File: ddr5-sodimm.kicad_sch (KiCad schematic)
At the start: 0 parts

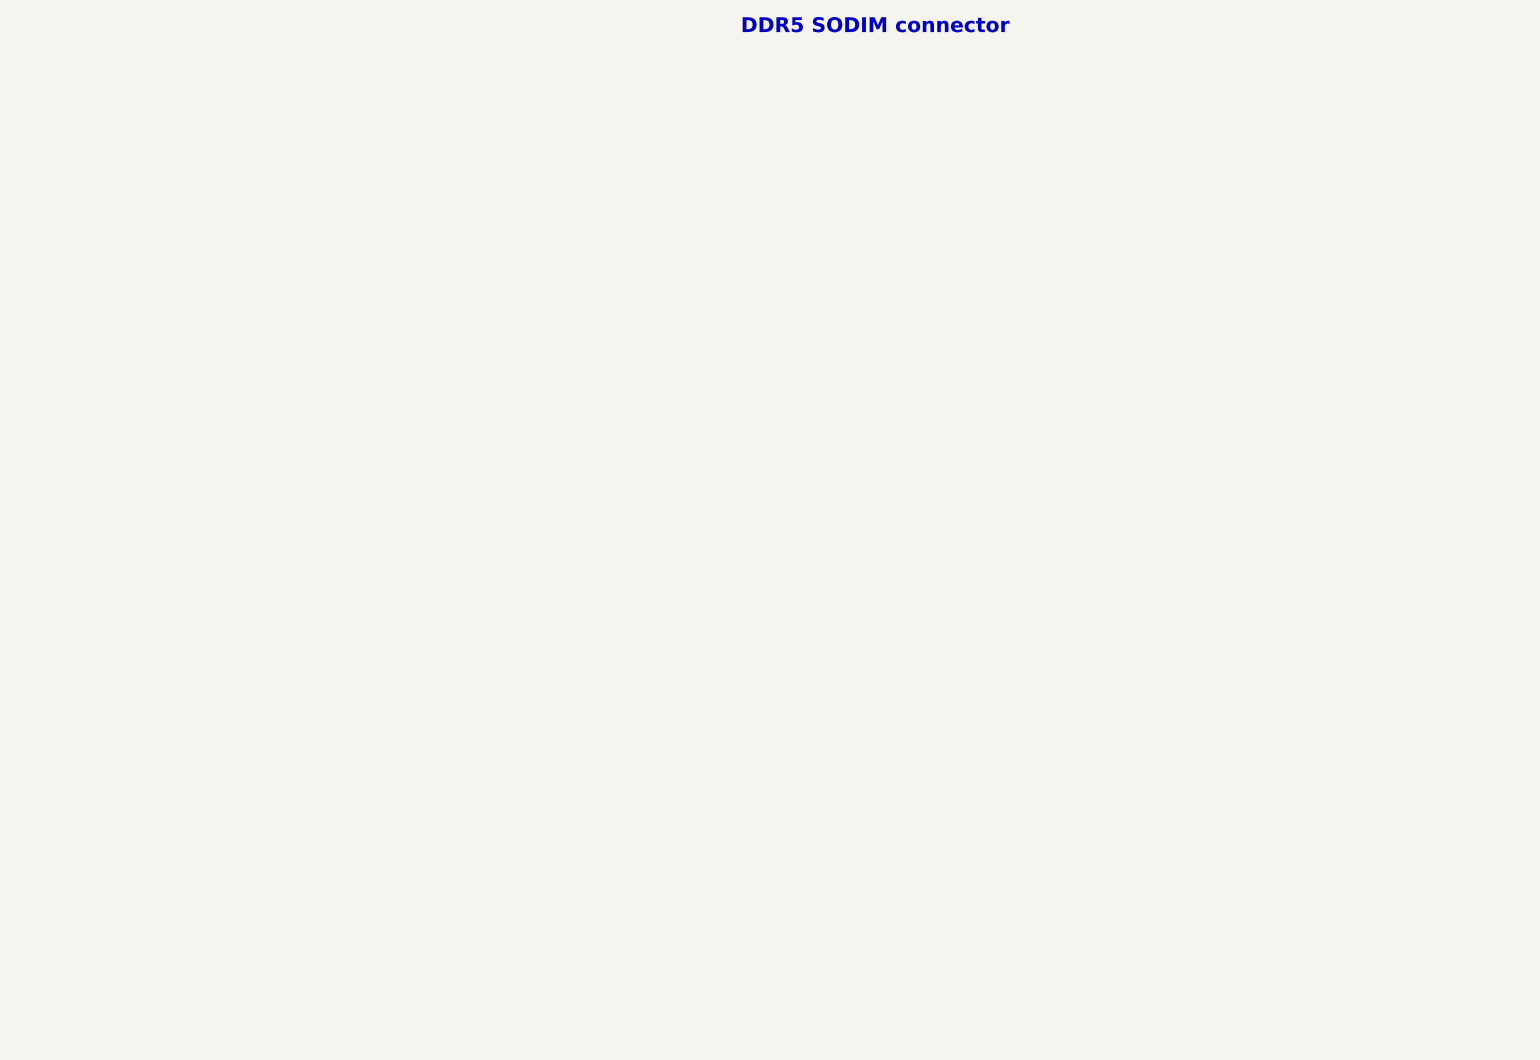
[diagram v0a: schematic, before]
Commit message: Add DDR5 connector to the schematic
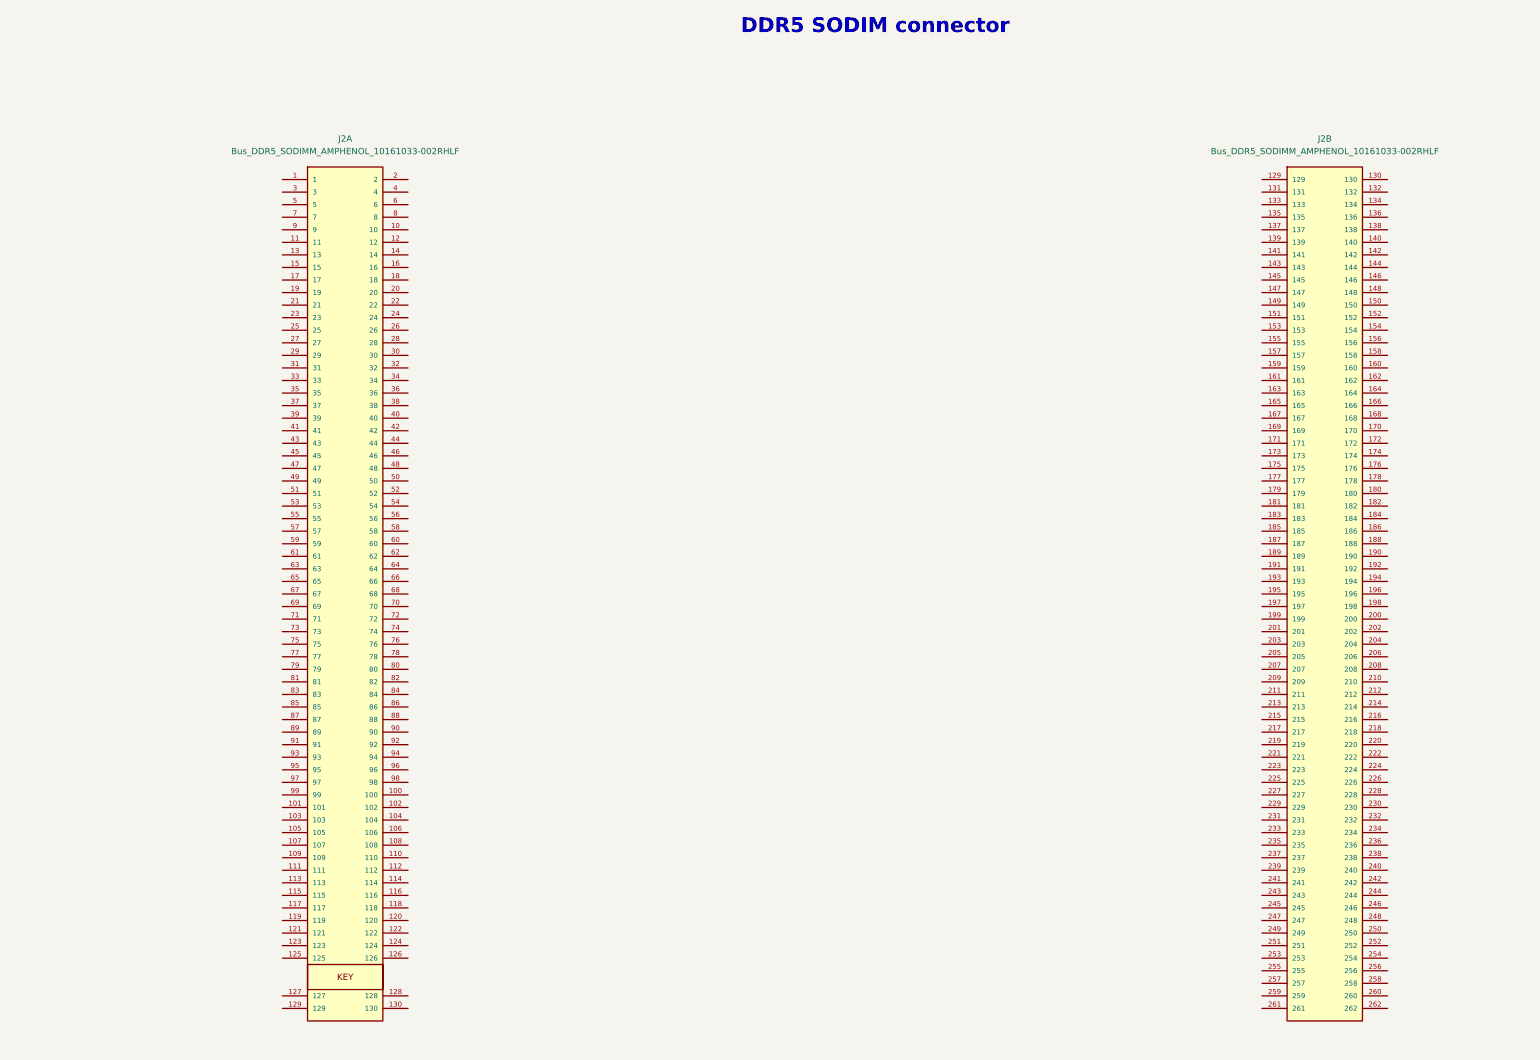
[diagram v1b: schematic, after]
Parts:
- added J2: Bus_DDR5_SODIMM_AMPHENOL_10161033-002RHLF, antmicro-footprints:DDR5_AMPHENOL_10161033-002RHLF, symbol antmicroMemoryConnectorsPCCardSockets:Bus_DDR5_SODIMM_AMPHENOL_10161033-002RHLF

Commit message: Update DDR5 SO-DIMM symbol and connect signals
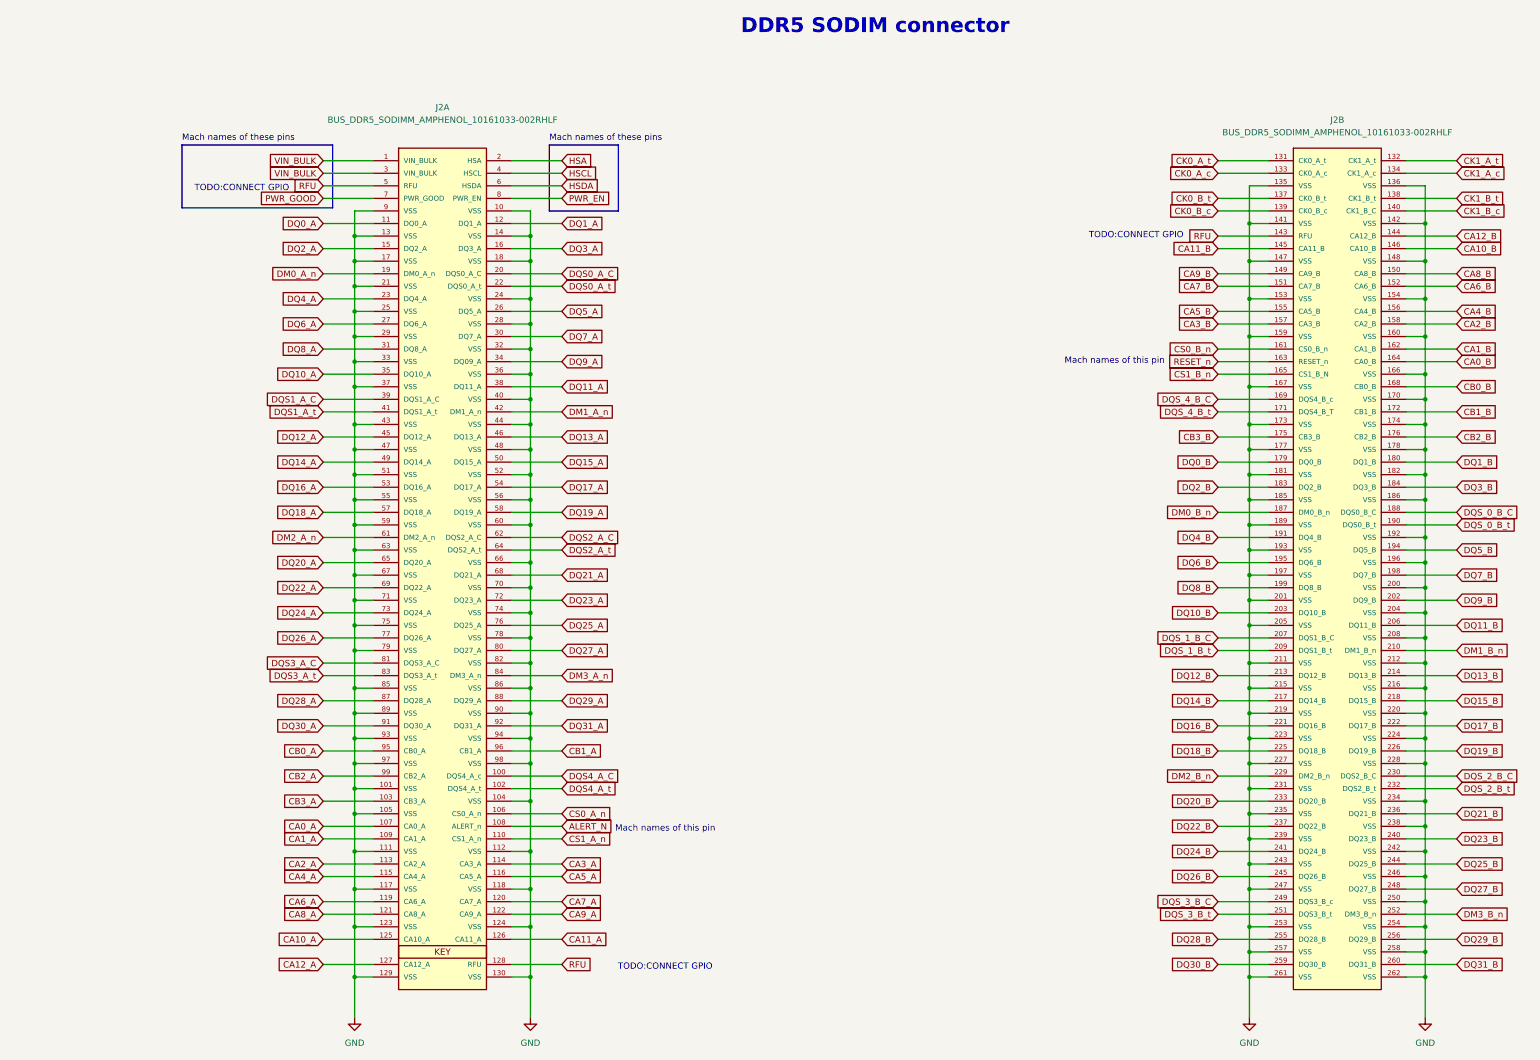
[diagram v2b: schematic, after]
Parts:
- removed J2: Bus_DDR5_SODIMM_AMPHENOL_10161033-002RHLF, antmicro-footprints:DDR5_AMPHENOL_10161033-002RHLF, symbol antmicroMemoryConnectorsPCCardSockets:Bus_DDR5_SODIMM_AMPHENOL_10161033-002RHLF
- added J2: BUS_DDR5_SODIMM_AMPHENOL_10161033-002RHLF, antmicro-footprints:DDR5_AMPHENOL_10161033-002RHLF, symbol antmicroMemoryConnectorsPCCardSockets:BUS_DDR5_SODIMM_AMPHENOL_10161033-002RHLF
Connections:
- new net ALERT_N: J2.108 (ALERT_n)
- new net CA0_A: J2.107 (CA0_A)
- new net CA0_B: J2.164 (CA0_B)
- new net CA10_A: J2.125 (CA10_A)
- new net CA10_B: J2.146 (CA10_B)
- new net CA11_A: J2.126 (CA11_A)
- new net CA11_B: J2.145 (CA11_B)
- new net CA12_A: J2.127 (CA12_A)
- new net CA12_B: J2.144 (CA12_B)
- new net CA1_A: J2.109 (CA1_A)
- new net CA1_B: J2.162 (CA1_B)
- new net CA2_A: J2.113 (CA2_A)
- new net CA2_B: J2.158 (CA2_B)
- new net CA3_A: J2.114 (CA3_A)
- new net CA3_B: J2.157 (CA3_B)
- new net CA4_A: J2.115 (CA4_A)
- new net CA4_B: J2.156 (CA4_B)
- new net CA5_A: J2.116 (CA5_A)
- new net CA5_B: J2.155 (CA5_B)
- new net CA6_A: J2.119 (CA6_A)
- new net CA6_B: J2.152 (CA6_B)
- new net CA7_A: J2.120 (CA7_A)
- new net CA7_B: J2.151 (CA7_B)
- new net CA8_A: J2.121 (CA8_A)
- new net CA8_B: J2.150 (CA8_B)
- new net CA9_A: J2.122 (CA9_A)
- new net CA9_B: J2.149 (CA9_B)
- new net CB0_A: J2.95 (CB0_A)
- new net CB0_B: J2.168 (CB0_B)
- new net CB1_A: J2.96 (CB1_A)
- new net CB1_B: J2.172 (CB1_B)
- new net CB2_A: J2.99 (CB2_A)
- new net CB2_B: J2.176 (CB2_B)
- new net CB3_A: J2.103 (CB3_A)
- new net CB3_B: J2.175 (CB3_B)
- new net CK0_A_c: J2.133 (CK0_A_c)
- new net CK0_A_t: J2.131 (CK0_A_t)
- new net CK0_B_c: J2.139 (CK0_B_c)
- new net CK0_B_t: J2.137 (CK0_B_t)
- new net CK1_A_c: J2.134 (CK1_A_c)
- new net CK1_A_t: J2.132 (CK1_A_t)
- new net CK1_B_c: J2.140 (CK1_B_C)
- new net CK1_B_t: J2.138 (CK1_B_t)
- new net CS0_A_n: J2.106 (CS0_A_n)
- new net CS0_B_n: J2.161 (CS0_B_n)
- new net CS1_A_n: J2.110 (CS1_A_n)
- new net CS1_B_n: J2.165 (CS1_B_N)
- new net DM0_A_n: J2.19 (DM0_A_n)
- new net DM0_B_n: J2.187 (DM0_B_n)
- new net DM1_A_n: J2.42 (DM1_A_n)
- new net DM1_B_n: J2.210 (DM1_B_n)
- new net DM2_A_n: J2.61 (DM2_A_n)
- new net DM2_B_n: J2.229 (DM2_B_n)
- new net DM3_A_n: J2.84 (DM3_A_n)
- new net DM3_B_n: J2.252 (DM3_B_n)
- new net DQ0_A: J2.11 (DQ0_A)
- new net DQ0_B: J2.179 (DQ0_B)
- new net DQ10_A: J2.35 (DQ10_A)
- new net DQ10_B: J2.203 (DQ10_B)
- new net DQ11_A: J2.38 (DQ11_A)
- new net DQ11_B: J2.206 (DQ11_B)
- new net DQ12_A: J2.45 (DQ12_A)
- new net DQ12_B: J2.213 (DQ12_B)
- new net DQ13_A: J2.46 (DQ13_A)
- new net DQ13_B: J2.214 (DQ13_B)
- new net DQ14_A: J2.49 (DQ14_A)
- new net DQ14_B: J2.217 (DQ14_B)
- new net DQ15_A: J2.50 (DQ15_A)
- new net DQ15_B: J2.218 (DQ15_B)
- new net DQ16_A: J2.53 (DQ16_A)
- new net DQ16_B: J2.221 (DQ16_B)
- new net DQ17_A: J2.54 (DQ17_A)
- new net DQ17_B: J2.222 (DQ17_B)
- new net DQ18_A: J2.57 (DQ18_A)
- new net DQ18_B: J2.225 (DQ18_B)
- new net DQ19_A: J2.58 (DQ19_A)
- new net DQ19_B: J2.226 (DQ19_B)
- new net DQ1_A: J2.12 (DQ1_A)
- new net DQ1_B: J2.180 (DQ1_B)
- new net DQ20_A: J2.65 (DQ20_A)
- new net DQ20_B: J2.233 (DQ20_B)
- new net DQ21_A: J2.68 (DQ21_A)
- new net DQ21_B: J2.236 (DQ21_B)
- new net DQ22_A: J2.69 (DQ22_A)
- new net DQ22_B: J2.237 (DQ22_B)
- new net DQ23_A: J2.72 (DQ23_A)
- new net DQ23_B: J2.240 (DQ23_B)
- new net DQ24_A: J2.73 (DQ24_A)
- new net DQ24_B: J2.241 (DQ24_B)
- new net DQ25_A: J2.76 (DQ25_A)
- new net DQ25_B: J2.244 (DQ25_B)
- new net DQ26_A: J2.77 (DQ26_A)
- new net DQ26_B: J2.245 (DQ26_B)
- new net DQ27_A: J2.80 (DQ27_A)
- new net DQ27_B: J2.248 (DQ27_B)
- new net DQ28_A: J2.87 (DQ28_A)
- new net DQ28_B: J2.255 (DQ28_B)
- new net DQ29_A: J2.88 (DQ29_A)
- new net DQ29_B: J2.256 (DQ29_B)
- new net DQ2_A: J2.15 (DQ2_A)
- new net DQ2_B: J2.183 (DQ2_B)
- new net DQ30_A: J2.91 (DQ30_A)
- new net DQ30_B: J2.259 (DQ30_B)
- new net DQ31_A: J2.92 (DQ31_A)
- new net DQ31_B: J2.260 (DQ31_B)
- new net DQ3_A: J2.16 (DQ3_A)
- new net DQ3_B: J2.184 (DQ3_B)
- new net DQ4_A: J2.23 (DQ4_A)
- new net DQ4_B: J2.191 (DQ4_B)
- new net DQ5_A: J2.26 (DQ5_A)
- new net DQ5_B: J2.194 (DQ5_B)
- new net DQ6_A: J2.27 (DQ6_A)
- new net DQ6_B: J2.195 (DQ6_B)
- new net DQ7_A: J2.30 (DQ7_A)
- new net DQ7_B: J2.198 (DQ7_B)
- new net DQ8_A: J2.31 (DQ8_A)
- new net DQ8_B: J2.199 (DQ8_B)
- new net DQ9_A: J2.34 (DQ09_A)
- new net DQ9_B: J2.202 (DQ9_B)
- new net DQS0_A_C: J2.20 (DQS0_A_C)
- new net DQS0_A_t: J2.22 (DQS0_A_t)
- new net DQS1_A_C: J2.39 (DQS1_A_C)
- new net DQS1_A_t: J2.41 (DQS1_A_t)
- new net DQS2_A_C: J2.62 (DQS2_A_C)
- new net DQS2_A_t: J2.64 (DQS2_A_t)
- new net DQS3_A_C: J2.81 (DQS3_A_C)
- new net DQS3_A_t: J2.83 (DQS3_A_t)
- new net DQS4_A_C: J2.100 (DQS4_A_c)
- new net DQS4_A_t: J2.102 (DQS4_A_t)
- new net DQS_0_B_C: J2.188 (DQS0_B_C)
- new net DQS_0_B_t: J2.190 (DQS0_B_t)
- new net DQS_1_B_C: J2.207 (DQS1_B_C)
- new net DQS_1_B_t: J2.209 (DQS1_B_t)
- new net DQS_2_B_C: J2.230 (DQS2_B_C)
- new net DQS_2_B_t: J2.232 (DQS2_B_t)
- new net DQS_3_B_C: J2.249 (DQS3_B_c)
- new net DQS_3_B_t: J2.251 (DQS3_B_t)
- new net DQS_4_B_C: J2.169 (DQS4_B_c)
- new net DQS_4_B_t: J2.171 (DQS4_B_T)
- new net GND: J2.10 (VSS), J2.101 (VSS), J2.104 (VSS), J2.105 (VSS), J2.111 (VSS), J2.112 (VSS), J2.117 (VSS), J2.118 (VSS), J2.123 (VSS), J2.124 (VSS), J2.129 (VSS), J2.13 (VSS), J2.130 (VSS), J2.135 (VSS), J2.136 (VSS), J2.14 (VSS), J2.141 (VSS), J2.142 (VSS), J2.147 (VSS), J2.148 (VSS), J2.153 (VSS), J2.154 (VSS), J2.159 (VSS), J2.160 (VSS), J2.166 (VSS), J2.167 (VSS), J2.17 (VSS), J2.170 (VSS), J2.173 (VSS), J2.174 (VSS), J2.177 (VSS), J2.178 (VSS), J2.18 (VSS), J2.181 (VSS), J2.182 (VSS), J2.185 (VSS), J2.186 (VSS), J2.189 (VSS), J2.192 (VSS), J2.193 (VSS), J2.196 (VSS), J2.197 (VSS), J2.200 (VSS), J2.201 (VSS), J2.204 (VSS), J2.205 (VSS), J2.208 (VSS), J2.21 (VSS), J2.211 (VSS), J2.212 (VSS), J2.215 (VSS), J2.216 (VSS), J2.219 (VSS), J2.220 (VSS), J2.223 (VSS), J2.224 (VSS), J2.227 (VSS), J2.228 (VSS), J2.231 (VSS), J2.234 (VSS), J2.235 (VSS), J2.238 (VSS), J2.239 (VSS), J2.24 (VSS), J2.242 (VSS), J2.243 (VSS), J2.246 (VSS), J2.247 (VSS), J2.25 (VSS), J2.250 (VSS), J2.253 (VSS), J2.254 (VSS), J2.257 (VSS), J2.258 (VSS), J2.261 (VSS), J2.262 (VSS), J2.28 (VSS), J2.29 (VSS), J2.32 (VSS), J2.33 (VSS), J2.36 (VSS), J2.37 (VSS), J2.40 (VSS), J2.43 (VSS), J2.44 (VSS), J2.47 (VSS), J2.48 (VSS), J2.51 (VSS), J2.52 (VSS), J2.55 (VSS), J2.56 (VSS), J2.59 (VSS), J2.60 (VSS), J2.63 (VSS), J2.66 (VSS), J2.67 (VSS), J2.70 (VSS), J2.71 (VSS), J2.74 (VSS), J2.75 (VSS), J2.78 (VSS), J2.79 (VSS), J2.82 (VSS), J2.85 (VSS), J2.86 (VSS), J2.89 (VSS), J2.9 (VSS), J2.90 (VSS), J2.93 (VSS), J2.94 (VSS), J2.97 (VSS), J2.98 (VSS)
- new net HSA: J2.2 (HSA)
- new net HSCL: J2.4 (HSCL)
- new net HSDA: J2.6 (HSDA)
- new net PWR_EN: J2.8 (PWR_EN)
- new net PWR_GOOD: J2.7 (PWR_GOOD)
- new net RESET_n: J2.163 (RESET_n)
- new net RFU: J2.128 (RFU), J2.143 (RFU), J2.5 (RFU)
- new net VIN_BULK: J2.1 (VIN_BULK), J2.3 (VIN_BULK)
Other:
- note added: "Mach names of these pins"
- note added: "Mach names of this pin"
- note added: "TODO:CONNECT GPIO"

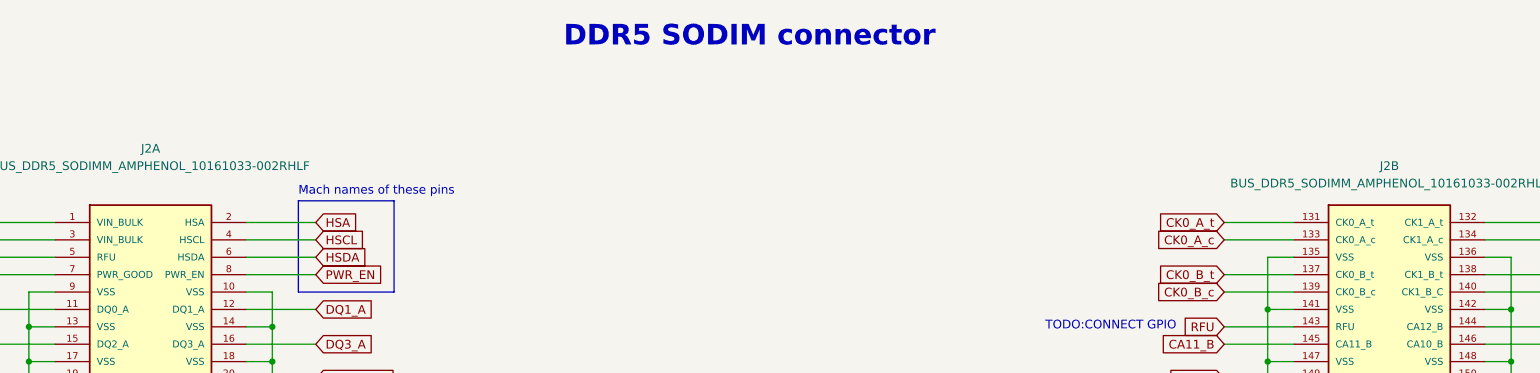
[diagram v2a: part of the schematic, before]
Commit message: Update designators and sync schematic with PCB
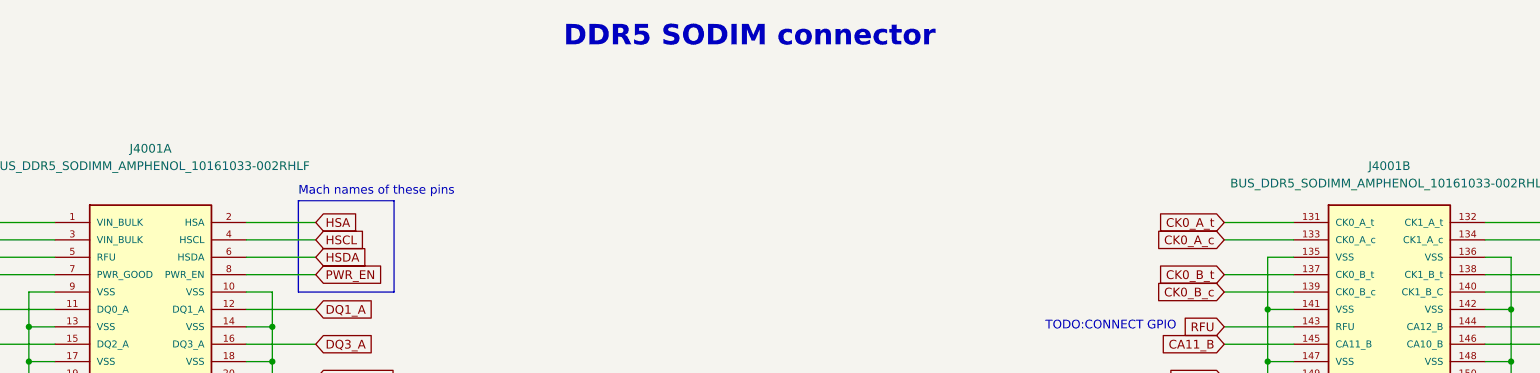
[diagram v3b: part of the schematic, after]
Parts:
- renumbered J2 to J4001
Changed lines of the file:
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@@
   (symbol (lib_id "data-center-rdimm-ddr4-tester:GND") (at 276.86 224.79 0) (unit 1)
     (in_bom yes) (on_board yes) (fields_autoplaced)
-    (property "Reference" "#PWR?" (id 0) (at 276.86 231.14 0)
+    (property "Reference" "#PWR04003" (id 0) (at 276.86 231.14 0)
       (effects (font (size 1.27 1.27)) hide)
     )
@@
   (symbol (lib_id "data-center-rdimm-ddr4-tester:GND") (at 95.885 224.79 0) (unit 1)
     (in_bom yes) (on_board yes) (fields_autoplaced)
-    (property "Reference" "#PWR?" (id 0) (at 95.885 231.14 0)
+    (property "Reference" "#PWR04001" (id 0) (at 95.885 231.14 0)
       (effects (font (size 1.27 1.27)) hide)
     )
@@
   (symbol (lib_name "BUS_DDR5_SODIMM_AMPHENOL_10161033-002RHLF_1") (lib_id "antmicroMemoryConnectorsPCCardSockets:BUS_DDR5_SODIMM_AMPHENOL_10161033-002RHLF") (at 294.64 130.175 0) (unit 2)
     (in_bom yes) (on_board yes) (fields_autoplaced)
-    (property "Reference" "J2" (id 0) (at 294.64 43.18 0))
+    (property "Reference" "J4001" (id 0) (at 294.64 43.18 0))
     (property "Value" "BUS_DDR5_SODIMM_AMPHENOL_10161033-002RHLF" (id 1) (at 294.64 45.72 0))
     (property "Footprint" "antmicro-footprints:DDR5_AMPHENOL_10161033-002RHLF" (id 2) (at 369.57 57.785 0)
@@
   (symbol (lib_id "antmicroMemoryConnectorsPCCardSockets:BUS_DDR5_SODIMM_AMPHENOL_10161033-002RHLF") (at 113.665 130.175 0) (unit 1)
     (in_bom yes) (on_board yes) (fields_autoplaced)
-    (property "Reference" "J2" (id 0) (at 113.665 40.64 0))
+    (property "Reference" "J4001" (id 0) (at 113.665 40.64 0))
     (property "Value" "BUS_DDR5_SODIMM_AMPHENOL_10161033-002RHLF" (id 1) (at 113.665 43.18 0))
     (property "Footprint" "antmicro-footprints:DDR5_AMPHENOL_10161033-002RHLF" (id 2) (at 188.595 57.785 0)
@@
   (symbol (lib_id "data-center-rdimm-ddr4-tester:GND") (at 131.445 224.79 0) (unit 1)
     (in_bom yes) (on_board yes) (fields_autoplaced)
-    (property "Reference" "#PWR?" (id 0) (at 131.445 231.14 0)
+    (property "Reference" "#PWR04002" (id 0) (at 131.445 231.14 0)
       (effects (font (size 1.27 1.27)) hide)
     )
@@
   (symbol (lib_id "data-center-rdimm-ddr4-tester:GND") (at 312.42 224.79 0) (unit 1)
     (in_bom yes) (on_board yes) (fields_autoplaced)
-    (property "Reference" "#PWR?" (id 0) (at 312.42 231.14 0)
-      (effects (font (size 1.27 1.27)) hide)
-    )
+    (property "Reference" "#PWR04004" (id 0) (at 312.42 231.14 0)
+      (effects (font (size 1.27 1.27)) hide)
+    )
